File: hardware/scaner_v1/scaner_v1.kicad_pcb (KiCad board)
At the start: 2 copper layers, 41 x 58 mm, 43 parts, among them J1 OBD кабель, Q1 IRFB4110, U1 LM2596S-ADJ, U2 SN65HVD230, U3 SN65HVD230, U4 XIAO_ESP32C5

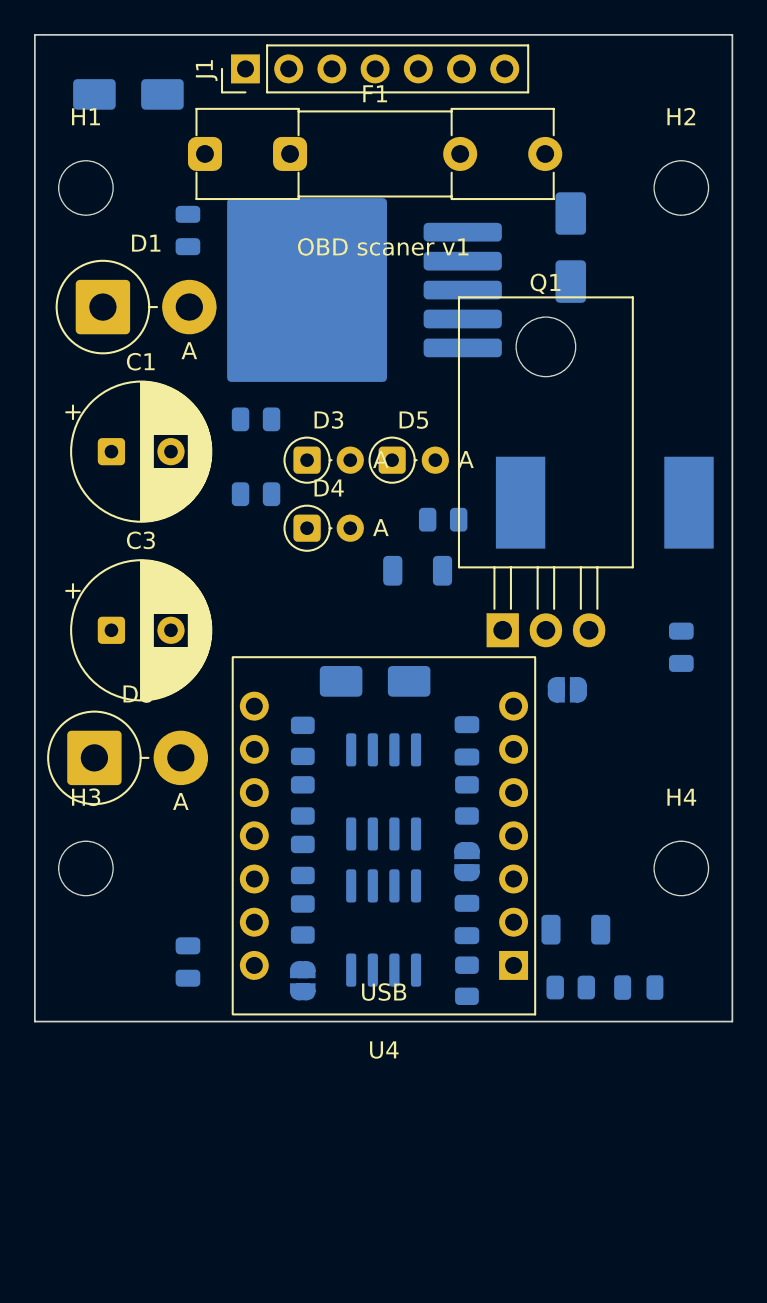
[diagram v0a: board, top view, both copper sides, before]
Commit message: PCB: 40 x 70 mm outline, holes 35 x 40 mm
Re-placed the draft layout for the measured enclosure size.
DRC clean except silkscreen; still unrouted.

Co-Authored-By: Claude Opus 5.5 <noreply@anthropic.com>
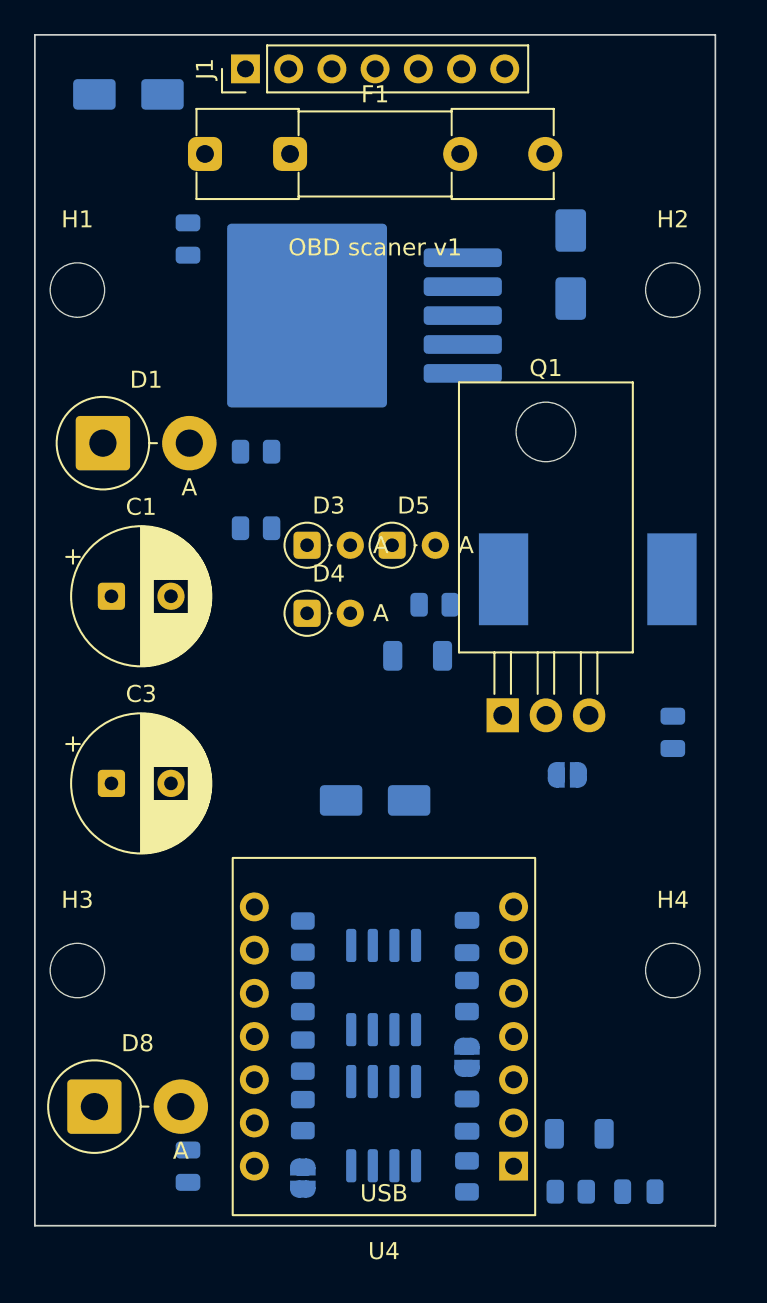
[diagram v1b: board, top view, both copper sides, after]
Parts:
- moved D8 20.5 mm to (103.5, 163.0)
- moved R9 12.0 mm to (132.0, 164.6)
- moved C5 12.0 mm to (109.0, 166.5)
- moved C8 12.0 mm to (135.5, 168.0)
- moved R10 12.0 mm to (131.5, 168.0)
- moved U4 11.8 mm to (128.1, 166.5)
- moved JP3 11.6 mm to (115.8, 167.2)
- moved C6 11.5 mm to (125.4, 153.0)
- moved C7 11.5 mm to (125.4, 163.5)
- moved JP2 11.5 mm to (125.4, 160.1)
- moved R11 11.5 mm to (115.8, 160.0)
- moved R12 11.5 mm to (115.8, 163.5)
- moved R5 11.5 mm to (115.8, 153.0)
- moved R6 11.5 mm to (115.8, 156.5)
- moved R7 11.5 mm to (125.4, 156.5)
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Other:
- board size 41 x 58 mm -> 40 x 70 mm

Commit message: Board v1: single-sided hand routing, 4-pin CAN connector, 3D models
- Tracks on bottom copper only, no wire jumpers; routes kept in
  tools/routes.py and laid by tools/hand_route.py, DRC clean
- THT pads 2.0 mm, 0.6 mm drills, SOIC pads 0.8 mm, solid GND pour
  with 1 mm clearance, no copper under the inductor
- J2 and J3 merged into one 4-pin CAN connector
- 12x12 inductor footprint with wide pads; VRML models for the XIAO
  on sockets, inductor, fuse holder and wire leads
- Firmware: new CAN pin map, TX held high and Rs released only after
  the controller starts (no pull-ups on the board)

Co-Authored-By: Claude Opus 5.5 <noreply@anthropic.com>
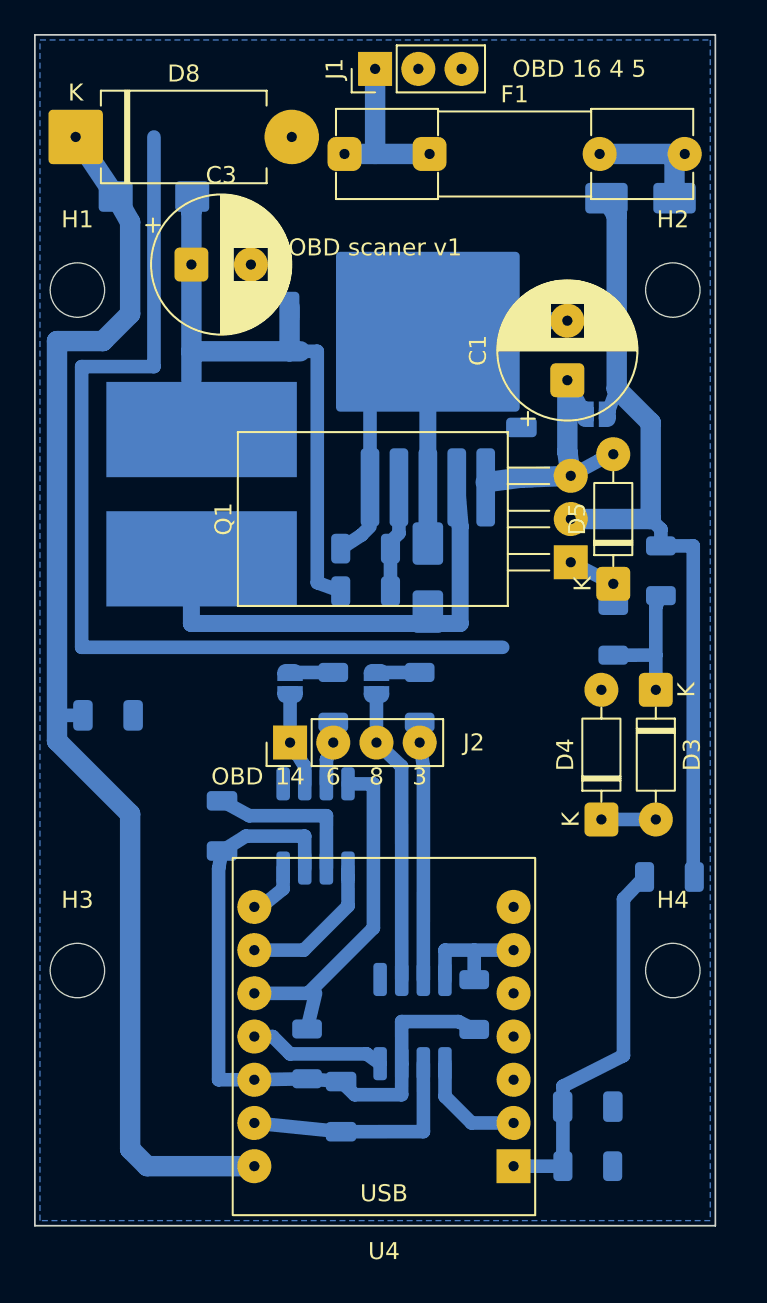
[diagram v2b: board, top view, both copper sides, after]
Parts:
- removed D1: 1.5KE27A, Diode_THT:D_DO-201AD_P5.08mm_Vertical_AnodeUp
- removed R5, R6: 10k, Resistor_SMD:R_0805_2012Metric
- added J2: OBD 14 6 8 3, Connector_PinHeader_2.54mm:PinHeader_1x04_P2.54mm_Vertical, F.Cu at (115.0, 141.6)
- C2, C4, C5, C6, C7, C8: footprint Capacitor_SMD:C_0805_2012Metric -> Capacitor_SMD:C_1206_3216Metric
- D3, D4, D5: footprint Diode_THT:D_DO-35_SOD27_P2.54mm_Vertical_AnodeUp -> Diode_THT:D_DO-35_SOD27_P7.62mm_Horizontal
- D8: footprint Diode_THT:D_DO-201AD_P5.08mm_Vertical_AnodeUp -> Diode_THT:D_DO-201AD_P12.70mm_Horizontal
- J1: value OBD кабель -> OBD питание; footprint Connector_PinHeader_2.54mm:PinHeader_1x07_P2.54mm_Vertical -> Connector_PinHeader_2.54mm:PinHeader_1x03_P2.54mm_Vertical
- L1: footprint Inductor_SMD:L_12x12mm_H4.5mm -> scaner:L_12x12mm_WidePads
- R10, R11, R12, R2, R3, R4, R7, R8: footprint Resistor_SMD:R_0805_2012Metric -> Resistor_SMD:R_1206_3216Metric
- moved D8 57.0 mm to (102.4, 106.0)
- moved D7 37.8 mm to (107.0, 109.5), turned to 0 degrees
- moved C4 34.7 mm to (113.5, 116.0), turned to 180 degrees
- moved C3 30.9 mm to (109.2, 113.5)
- moved D2 30.7 mm to (135.6, 109.6), turned to 0 degrees
- moved C1 29.7 mm to (131.3, 120.3), turned to 90 degrees
- moved JP3 29.4 mm to (120.1, 138.1), turned to -90 degrees
- moved R8 28.3 mm to (122.6, 138.9)
- moved C5 26.9 mm to (104.3, 140.0), turned to 0 degrees
- moved JP2 24.3 mm to (115.0, 138.1), turned to -90 degrees
- moved C2 23.3 mm to (128.6, 124.5)
- moved L1 23.2 mm to (109.8, 127.0), turned to 90 degrees
- moved D3 22.2 mm to (136.5, 138.5), turned to -90 degrees
- moved JP1 21.3 mm to (133.0, 122.3)
- moved D4 21.1 mm to (133.3, 146.1), turned to 90 degrees
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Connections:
- U4 pad 10: /CANA_RX -> /RS_A
- U4 pad 11: /CANA_TX -> /CANB_RX
- U4 pad 2: /CANB_RX -> /CANB_TX
- U4 pad 5: /RS_A -> unconnected-(U4-D4/GPIO23/SDA-Pad5)
- U4 pad 8: unconnected-(U4-D7/GPIO12/RX-Pad8) -> /CANA_RX
- U4 pad 9: /CANB_TX -> /CANA_TX
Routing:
- net GND: track 0.00 -> 97.8 mm
- net /V5: track 0.00 -> 74.8 mm
- net /VIN_PROT: track 0.00 -> 49.4 mm
- net /+3V3: track 0.00 -> 40.2 mm
- net /V5_BUCK: track 0.00 -> 35.9 mm
- net /SW: track 0.00 -> 24.8 mm
- net /VBAT_ADC: track 0.00 -> 22.6 mm
- net /RS_A: track 0.00 -> 20.7 mm
- net /CANB_L: track 0.00 -> 17.4 mm
- net /VIN_BUCK: track 0.00 -> 15.7 mm
- net /CANB_H: track 0.00 -> 15.1 mm
- net /VBAT_OBD: track 0.00 -> 10.0 mm
- net /CANA_TX: track 0.00 -> 8.81 mm
- net /GATE_REF: track 0.00 -> 8.10 mm
- net /CANB_RX: track 0.00 -> 8.00 mm
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- added copper zone on B.Cu, net GND
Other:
- board text added: "14"
- board text added: "3"
- board text added: "6"
- board text added: "8"
- board text added: "OBD"
- board text added: "OBD 16 4 5"
